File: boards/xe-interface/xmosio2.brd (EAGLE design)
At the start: 116.8 x 100 mm, 122 parts, among them IC1 IDTQS3245QSOP20, IC2 IDTQS3245QSOP20, IC3 IDTQS3245QSOP20, IC4 IDTQS3245QSOP20, IC5 IDTQS3245QSOP20, U1 24 MHz Osc. (F535L-24), U2 USD-SOCKETNEW, X1 0446200002

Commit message: Latest design changes  - Move the XTAG connector back significantly, so the shroud is not overhanging the board  - Use the SD card slot, not the micro-SD card, it’s easier to solder  - Fix the SD card pinouts  - Remove an unwanted pull-up on the SD card
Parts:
- removed R25: 10K, rcl:R1206
- removed U2: USD-SOCKETNEW, SparkFun-Connectors:MICRO-SD-SOCKET-PP
- added J1: (no value), InputOutputIO (rev17e):693063020911
- moved C42 102.4 mm to (113.3, 10.5), turned to 0 degrees
- moved C43 102.2 mm to (113.3, 13.7), turned to 0 degrees
- moved R14 101.6 mm to (108.3, 14.9)
- moved U$11 97.9 mm to (113.7, 18.4)
- moved C44 93.4 mm to (113.0, 22.5), turned to 180 degrees
- moved R15 34.8 mm to (35.9, 21.7), turned to 180 degrees
- moved BOOT_SW 14.7 mm to (5.08, 14.3), turned to 180 degrees
- moved R26 11.6 mm to (43.8, 15.2), turned to 0 degrees
- moved R2 9.86 mm to (76.2, 14.0), turned to 90 degrees
- moved R24 9.71 mm to (43.8, 19.1), turned to 180 degrees
- moved U$3 9.67 mm to (81.6, 14.9)
- moved C9 9.09 mm to (64.1, 21.0)
- moved C20 7.96 mm to (67.9, 21.0), turned to 270 degrees
- moved C10 6.87 mm to (71.8, 21.0)
- moved C16 6.35 mm to (75.6, 21.0)
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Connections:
- new net SDC_CD: U$2.84
- net GND: now also J1.3, J1.6, J1.GND1, J1.GND2, J1.GND3, J1.GND4; no longer R26.2, U2.6, U2.CD1, U2.CD2, U2.GND1, U2.GND3
- net SDC_CLK: now also U$2.64; no longer U$2.96, U2.5
- net SDC_CMD: now also U$2.63; no longer U$2.94, U2.3
- net SDC_D0: now also U$2.96; no longer R25.1, U$2.93, U2.7
- net SDC_D1: now also U$2.94; no longer U$2.92, U2.8
- net SDC_D2: now also U$2.93; no longer U$2.64, U2.1
- net SDC_D3: now also R26.2, U$2.92; no longer R26.1, U$2.63, U2.2
- net VCCIO: now also R26.1; no longer R25.2, U2.4
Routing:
- net JTAG_DN0: track 51.9 -> 46.8 mm
- net JTAG_UP1: track 30.7 -> 25.6 mm
- net JTAG_DN1: track 52.1 -> 47.0 mm
- net JTAG_UP0: track 35.7 -> 30.6 mm
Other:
- board text added: "GND"

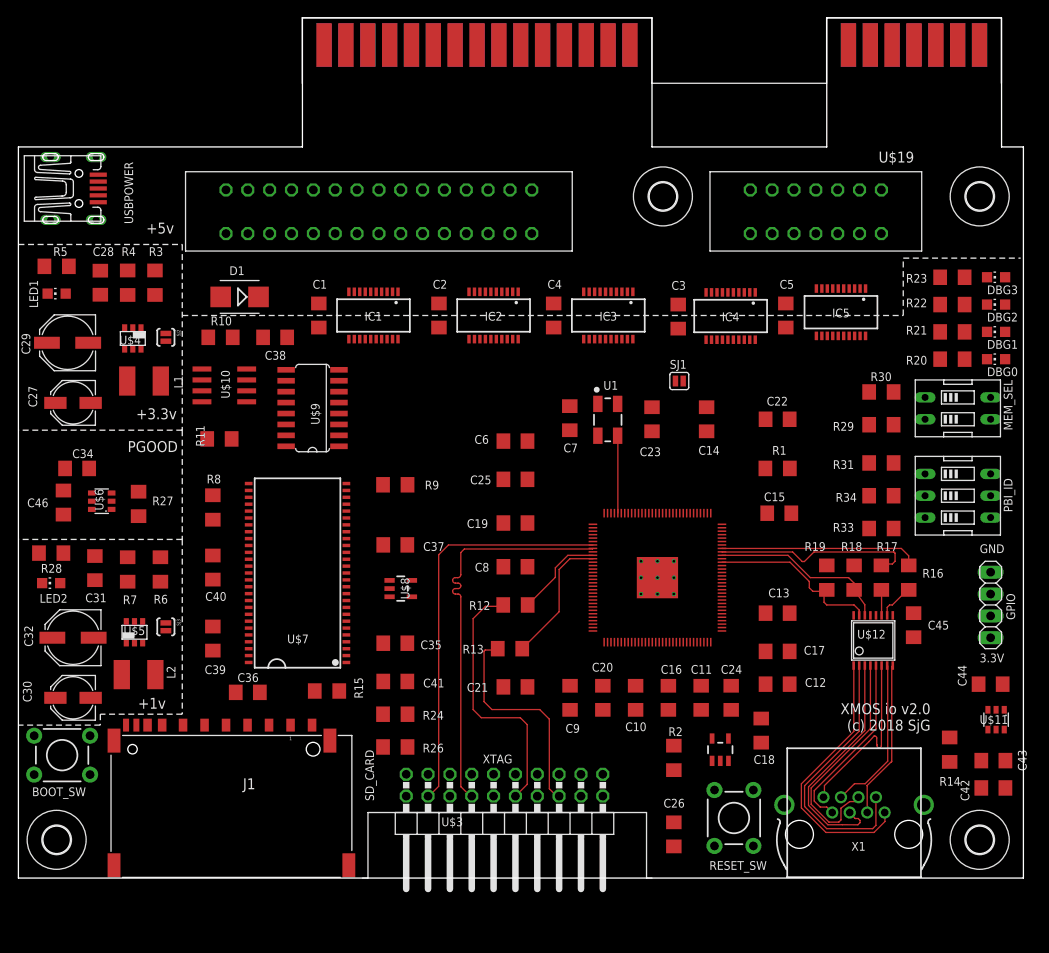
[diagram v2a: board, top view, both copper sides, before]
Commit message: - Fix the SD card so that the pins actually connect, even though they seem to be fine in the schematic  - Move some of the decoupling capacitors closer to the XMOS chip  - Provide JTAG +5V connection through pin header for manual selection  - Link up the 2 GPIO ports to the UART on the XTAG so they can be a serial connection during bringup  - Rotate the solder bridges on the power sections so they point the right way
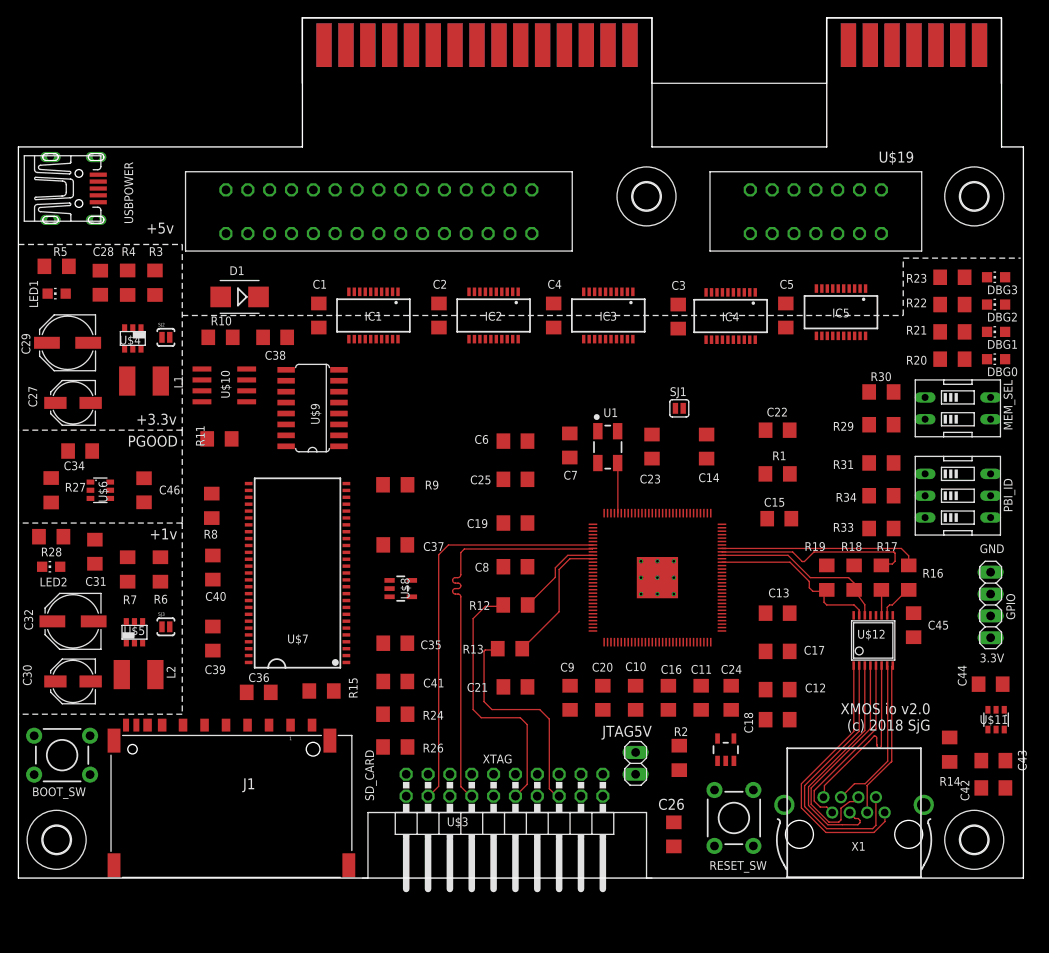
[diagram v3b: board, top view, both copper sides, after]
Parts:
- added JTAG5V: (no value), pinhead:1X02
- moved R27 10.3 mm to (3.81, 45.1)
- moved C46 9.47 mm to (14.6, 45.1), turned to 270 degrees
- moved C14 3.18 mm to (80.0, 50.2)
- moved C23 3.18 mm to (73.7, 50.2)
- moved C7 3.17 mm to (64.1, 50.3)
- moved SJ1 3.17 mm to (76.8, 54.6)
- moved U1 3.17 mm to (68.5, 50.1)
- moved C18 2.29 mm to (88.3, 18.4), turned to 180 degrees
- moved C34 2.05 mm to (7.17, 49.6), turned to 0 degrees
- moved C30 1.91 mm to (6.35, 22.9)
- moved H3 1.91 mm to (73.0, 79.2)
- moved LED2 1.91 mm to (3.81, 36.2)
- moved R28 1.91 mm to (3.81, 39.7)
- moved C32 1.90 mm to (6.35, 29.8)
- moved C31 1.90 mm to (8.89, 37.9)
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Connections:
- net N$21 renamed TRST_N
- removed net N$36: GPIO.3, U$2.12
- removed net N$37: GPIO.2, U$2.14
- new net N$38: JTAG5V.2, XTAG.1
- new net UART_RX: GPIO.2, U$2.14, XTAG.19
- new net UART_TX: GPIO.3, U$2.12, XTAG.17
- net +5V: now also JTAG5V.1
- net SDC_CD: now also J1.CD
- net SDC_CLK: now also J1.5
- net SDC_CMD: now also J1.2
- net SDC_D0: now also J1.7
- net SDC_D1: now also J1.8
- net SDC_D2: now also J1.9
- net SDC_D3: now also J1.1
- net VCCIO: now also J1.4
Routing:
- net N$2: track 9.01 -> 5.84 mm

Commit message: Fix or approve all the ERC warnings in the schematic. Fix all the DRC warnings
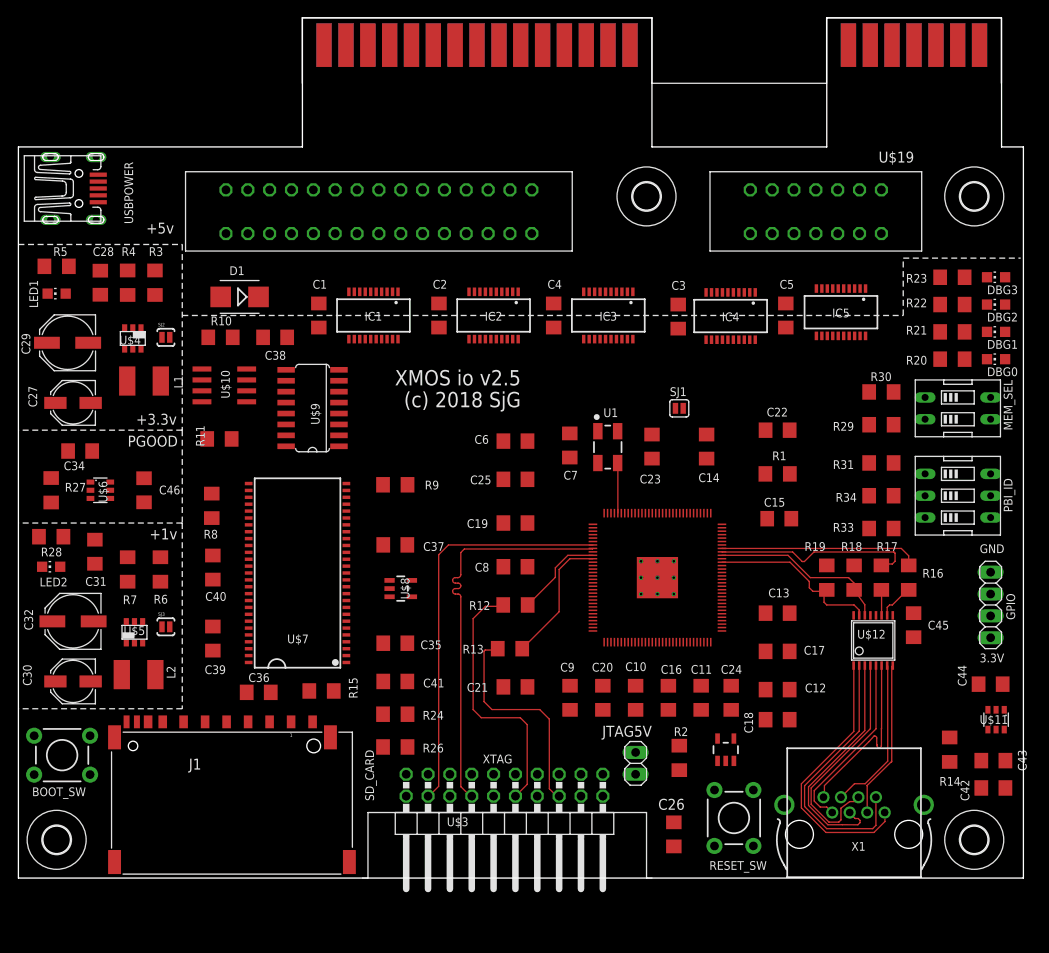
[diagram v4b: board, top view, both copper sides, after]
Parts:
- GPIO: value (none) -> UART
- J1: value (none) -> SD_CARD
- JTAG5V: value (none) -> PSU
- MEM_SEL: value (none) -> CT2092MS-ND
- PBI_ID: value (none) -> CT2093MS-ND
- moved J1 0.39 mm to (24.8, 18.2)
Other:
- board text added: "XMOS io v2.5"
- board text removed: "XMOS io v2.0"

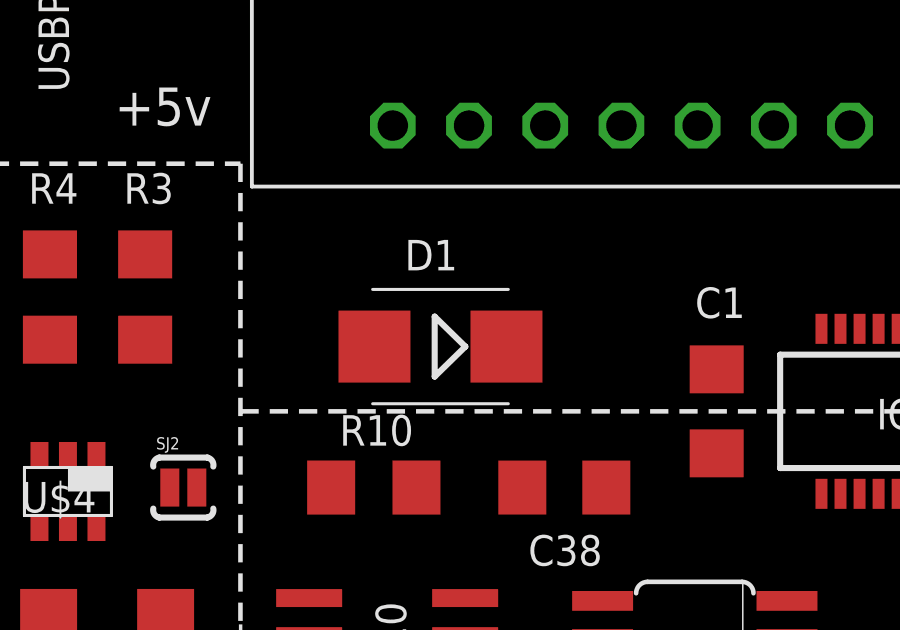
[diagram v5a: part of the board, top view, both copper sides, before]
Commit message: Use a 4N4001 diode (even though it’s through-hole) because the forward voltage drop of the original one was only 0.2v, and we actually want to use the diode to drop the voltage by 0.7v.
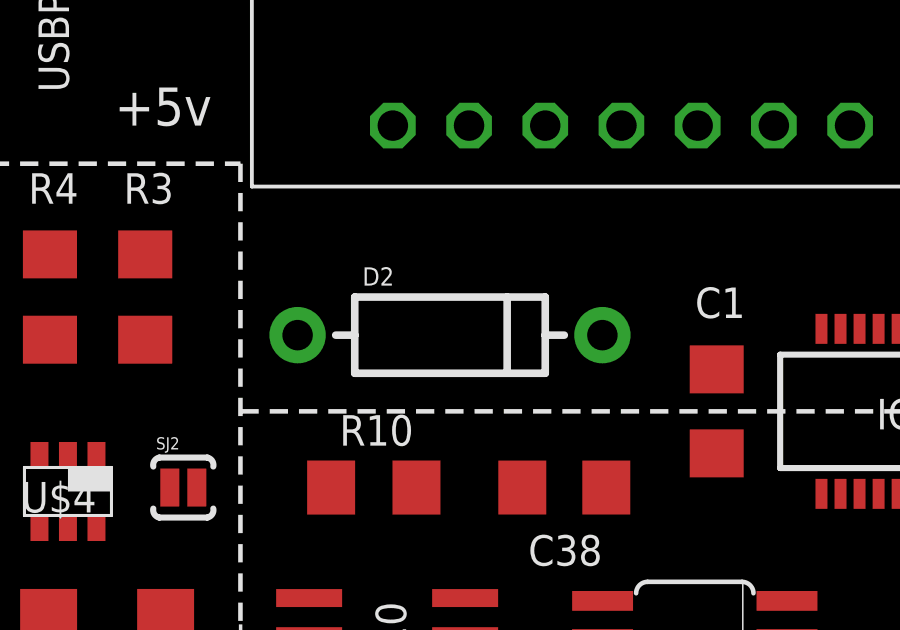
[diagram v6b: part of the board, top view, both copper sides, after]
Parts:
- removed D1: MURS120-E3, diode:SMB
- added D2: (no value), SparkFun-DiscreteSemi:DIODE-1N4001-KIT
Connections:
- net +4.3V: now also D2.C; no longer D1.C
- net +5V: now also D2.A; no longer D1.A
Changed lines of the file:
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@@
 <attribute name="VALUE" x="64.77" y="64.135" size="1.27" layer="27" rot="R90"/>
-</element>
-<element name="D1" library="diode" package="SMB" value="MURS120-E3" x="25.7175" y="67.564" smashed="yes" rot="R180">
-<attribute name="NAME" x="26.289" y="71.12" size="1.016" layer="25" rot="R180"/>
-<attribute name="VALUE" x="27.8765" y="70.993" size="1.27" layer="27" rot="R180"/>
 </element>
 <element name="U$2" library="Eagle_XMOS_Lib_COMPLETE" package="TQFP128" value="XL216-512-TQ128" x="74.295" y="34.925" smashed="yes"/>
@@
 <attribute name="VALUE" x="68.58" y="15.875" size="1.27" layer="27" rot="R270"/>
 </element>
+<element name="D2" library="SparkFun-DiscreteSemi" package="DIODE-1N4001-KIT" value="" x="26.035" y="67.945"/>
 </elements>
 <signals>
@@
 </signal>
 <signal name="+5V" class="1">
-<contactref element="D1" pad="A"/>
 <contactref element="U$4" pad="3"/>
 <contactref element="C27" pad="+"/>
@@
 <contactref element="U$19" pad="26"/>
 <contactref element="JTAG5V" pad="1"/>
+<contactref element="D2" pad="A"/>
 <wire x1="100.33" y1="80.01" x2="111.74" y2="96.845" width="0" layer="19" extent="16-16"/>
 <wire x1="66.02" y1="96.845" x2="100.33" y2="80.01" width="0" layer="19" extent="16-16"/>
 <wire x1="54.61" y1="80.01" x2="66.02" y2="96.845" width="0" layer="19" extent="16-16"/>
-<wire x1="23.5175" y1="67.564" x2="54.61" y2="80.01" width="0" layer="19" extent="1-1"/>
-<wire x1="12.35045625" y1="63.9839375" x2="23.5175" y2="67.564" width="0" layer="19" extent="1-1"/>
+<wire x1="12.35045625" y1="63.9839375" x2="54.61" y2="80.01" width="0" layer="19" extent="1-1"/>
 <wire x1="13.30045625" y1="61.4839375" x2="12.35045625" y2="63.9839375" width="0" layer="19" extent="1-1"/>
 <wire x1="4.3" y1="55.245" x2="13.30045625" y2="61.4839375" width="0" layer="19" extent="1-1"/>
@@
 <wire x1="14.44375" y1="27.325" x2="4.3" y2="55.245" width="0" layer="19" extent="1-1"/>
 <wire x1="4.3" y1="22.86" x2="14.44375" y2="27.325" width="0" layer="19" extent="1-1"/>
+<wire x1="20.955" y1="67.945" x2="4.3" y2="22.86" width="0" layer="19" extent="1-1"/>
 <wire x1="71.755" y1="14.605" x2="14.44375" y2="27.325" width="0" layer="19" extent="1-1"/>
 </signal>
@@
 </signal>
 <signal name="+4.3V">
-<contactref element="D1" pad="C"/>
 <contactref element="C2" pad="1"/>
 <contactref element="IC1" pad="20"/>
@@
 <contactref element="C4" pad="1"/>
 <contactref element="IC5" pad="20"/>
+<contactref element="D2" pad="C"/>
 <wire x1="89.2175" y1="64.005" x2="98.489" y2="63.036" width="0" layer="19" extent="1-1"/>
 <wire x1="85.662" y1="62.5915" x2="89.2175" y2="64.005" width="0" layer="19" extent="1-1"/>
@@
 <wire x1="44.133" y1="62.655" x2="48.895" y2="64.005" width="0" layer="19" extent="1-1"/>
 <wire x1="34.925" y1="64.005" x2="44.133" y2="62.655" width="0" layer="19" extent="1-1"/>
-<wire x1="27.9175" y1="67.564" x2="34.925" y2="64.005" width="0" layer="19" extent="1-1"/>
+<wire x1="31.115" y1="67.945" x2="34.925" y2="64.005" width="0" layer="19" extent="1-1"/>
 </signal>
 <signal name="N$10">

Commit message: Change the resistor value in the 1v power supply to 3.9k from 5.1k, which provides a better 1v supply.
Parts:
- R6: value 5K1 -> 3K9
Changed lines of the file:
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@@
 <attribute name="VALUE" x="6.985" y="38.57625" size="1.27" layer="27" rot="R270"/>
 </element>
-<element name="R6" library="rcl" package="R1206" value="5K1" x="16.51" y="35.8775" smashed="yes" rot="R270">
+<element name="R6" library="rcl" package="R1206" value="3K9" x="16.51" y="35.8775" smashed="yes" rot="R270">
 <attribute name="NAME" x="15.71625" y="31.90875" size="1.016" layer="25"/>
 <attribute name="VALUE" x="14.605" y="36.5125" size="1.27" layer="27" rot="R270"/>
